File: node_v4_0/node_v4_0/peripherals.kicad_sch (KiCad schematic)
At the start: 1 part, among them U6 RFM69HCW

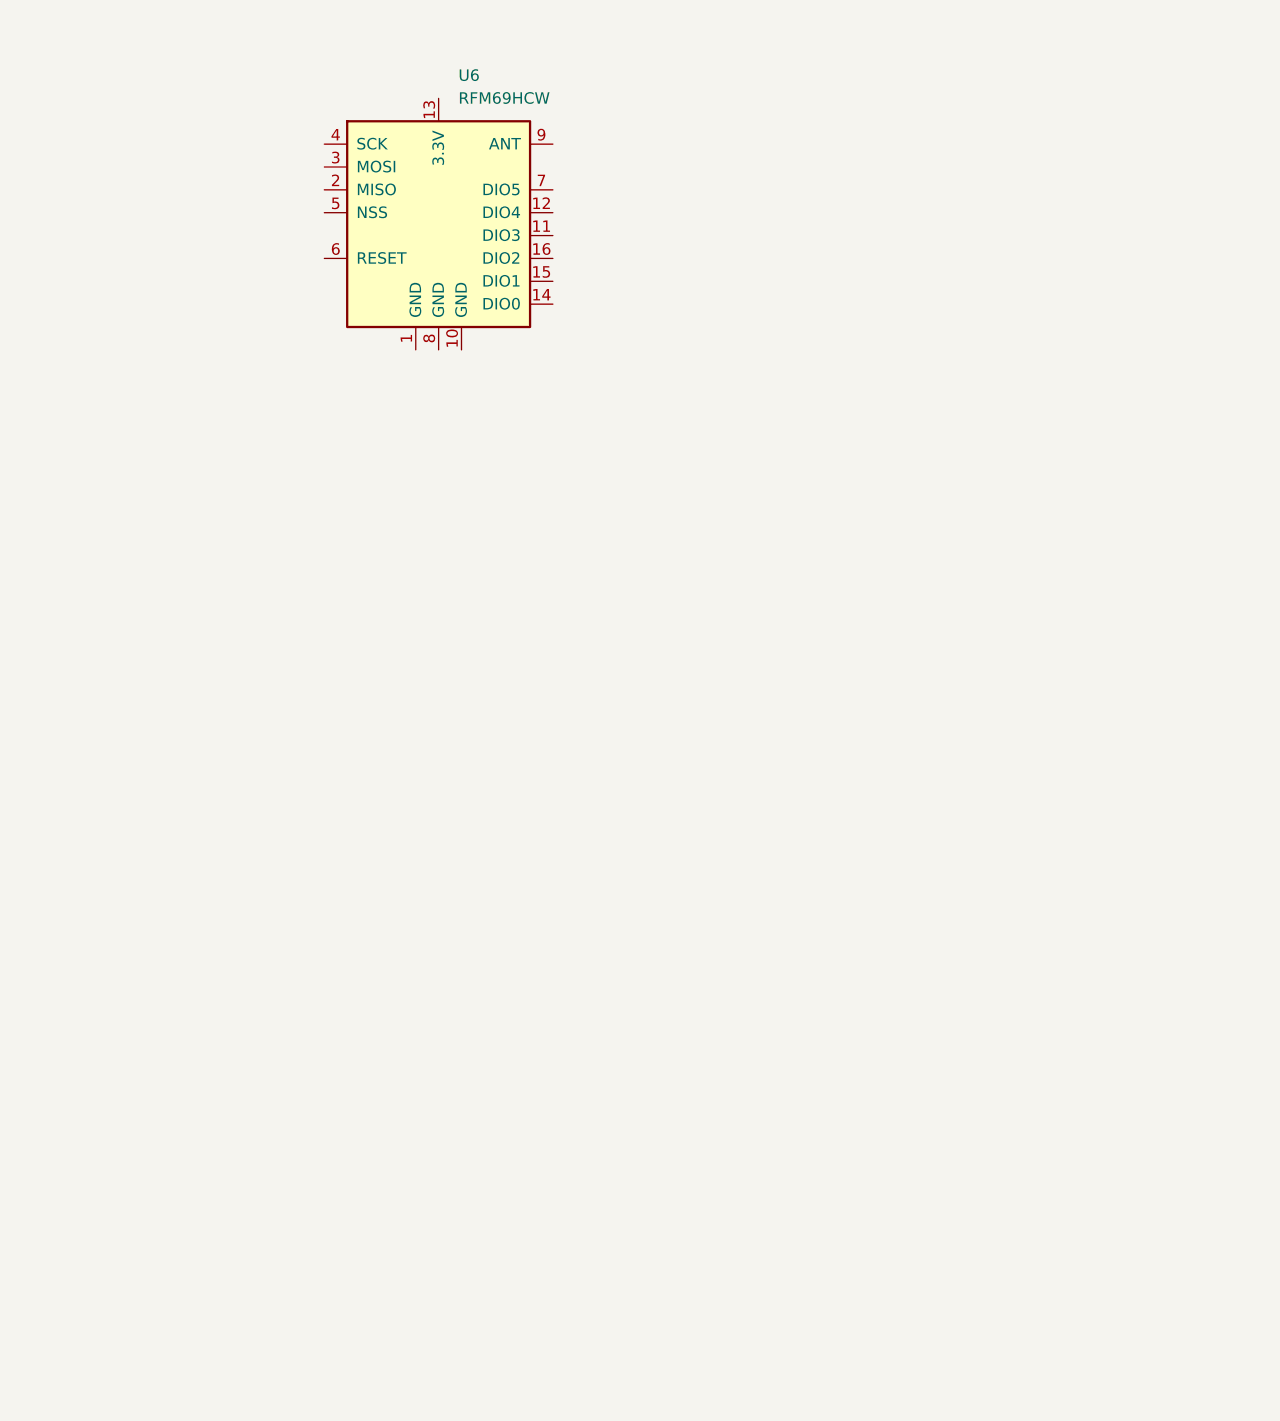
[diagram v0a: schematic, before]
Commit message: more tracing, added RFM, added SIM, built power systems. converted to star ground
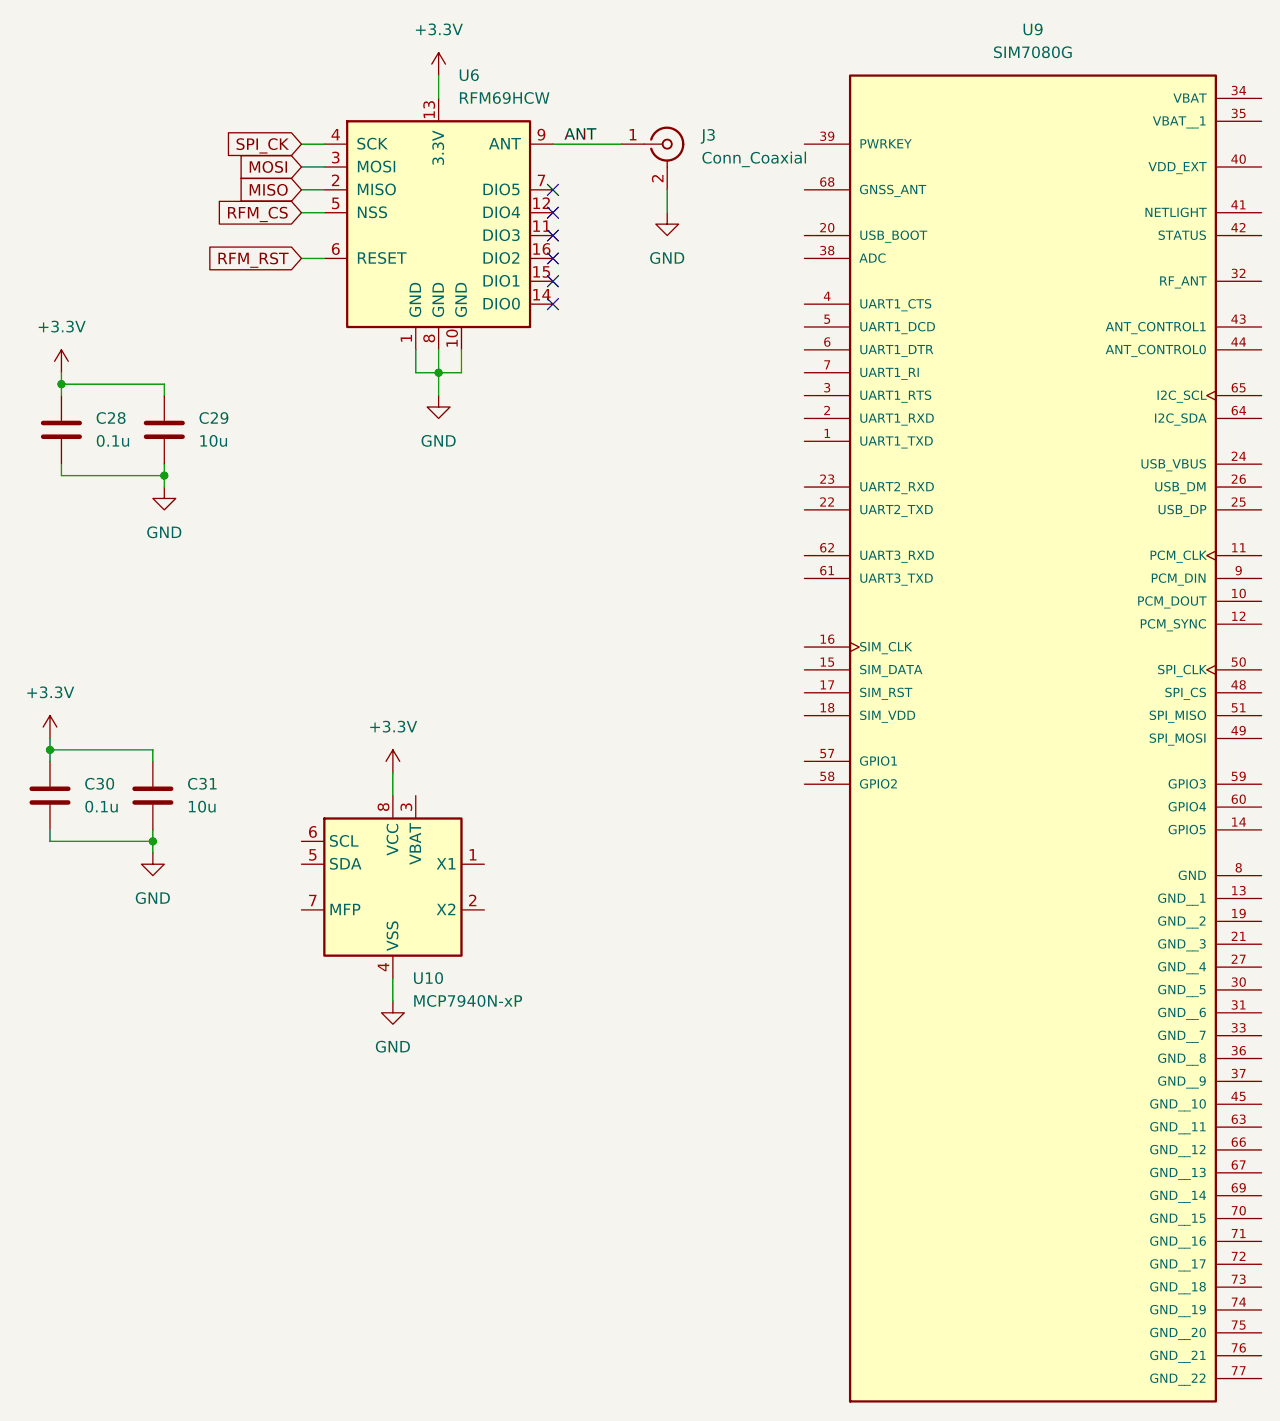
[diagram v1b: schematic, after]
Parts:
- added C28, C30: 0.1u, Capacitor_SMD:C_0402_1005Metric_Pad0.74x0.62mm_HandSolder, symbol Device:C
- added C29, C31: 10u, Capacitor_SMD:C_0805_2012Metric_Pad1.18x1.45mm_HandSolder, symbol Device:C
- added J3: Conn_Coaxial, Connector_Coaxial:SMA_Samtec_SMA-J-P-H-ST-EM1_EdgeMount, symbol Connector:Conn_Coaxial
- added U10: MCP7940N-xP, Package_SO:SOIC-8_3.9x4.9mm_P1.27mm, symbol Timer_RTC:MCP7940N-xP
- added U9: SIM7080G, Library:XCVR_SIM7080G, symbol SIM7080G:SIM7080G
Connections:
- net GND: now reaches U6.1 (GND)
- net GND: now also U6.10 (GND), U6.8 (GND), C28.2, C29.2, C30.2, C31.2, J3.2 (Ext), U10.4 (VSS)
- net +3.3V: now reaches U6.13 (3.3V)
- net +3.3V: now also C28.1, C29.1, C30.1, C31.1, U10.8 (VCC)
- net MISO: now reaches U6.2 (MISO)
- net MOSI: now reaches U6.3 (MOSI)
- net SPI_CK: now reaches U6.4 (SCK)
- net RFM_CS: now reaches U6.5 (NSS)
- net RFM_RST: now reaches U6.6 (RESET)
- net ANT: now reaches U6.9 (ANT)
- net ANT: now also J3.1 (In)
- no-connect marks 0 -> 6
